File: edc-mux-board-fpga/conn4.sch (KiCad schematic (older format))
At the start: 24 parts

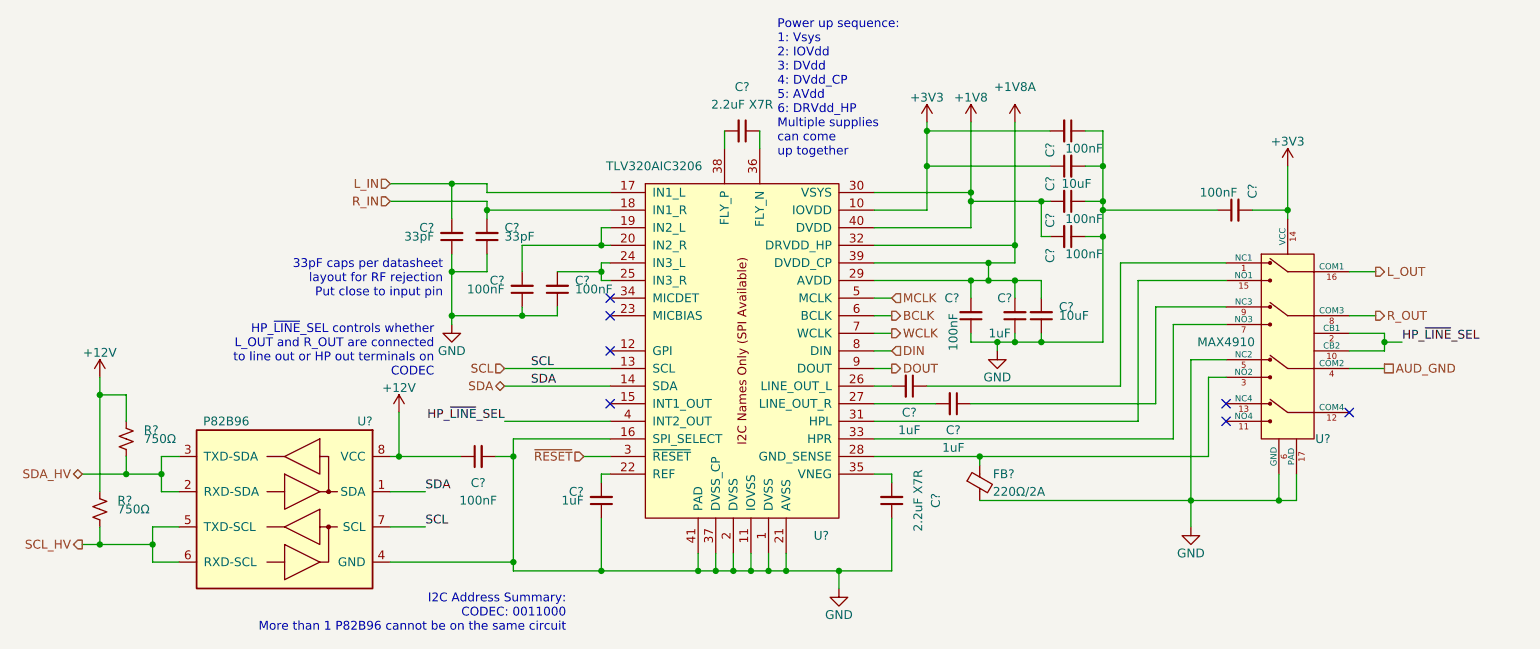
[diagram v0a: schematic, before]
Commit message: Finished FPGA and MCU interconnections.
Finished up interrupt wiring
Fixed a few missing connections
Annotated Schematic
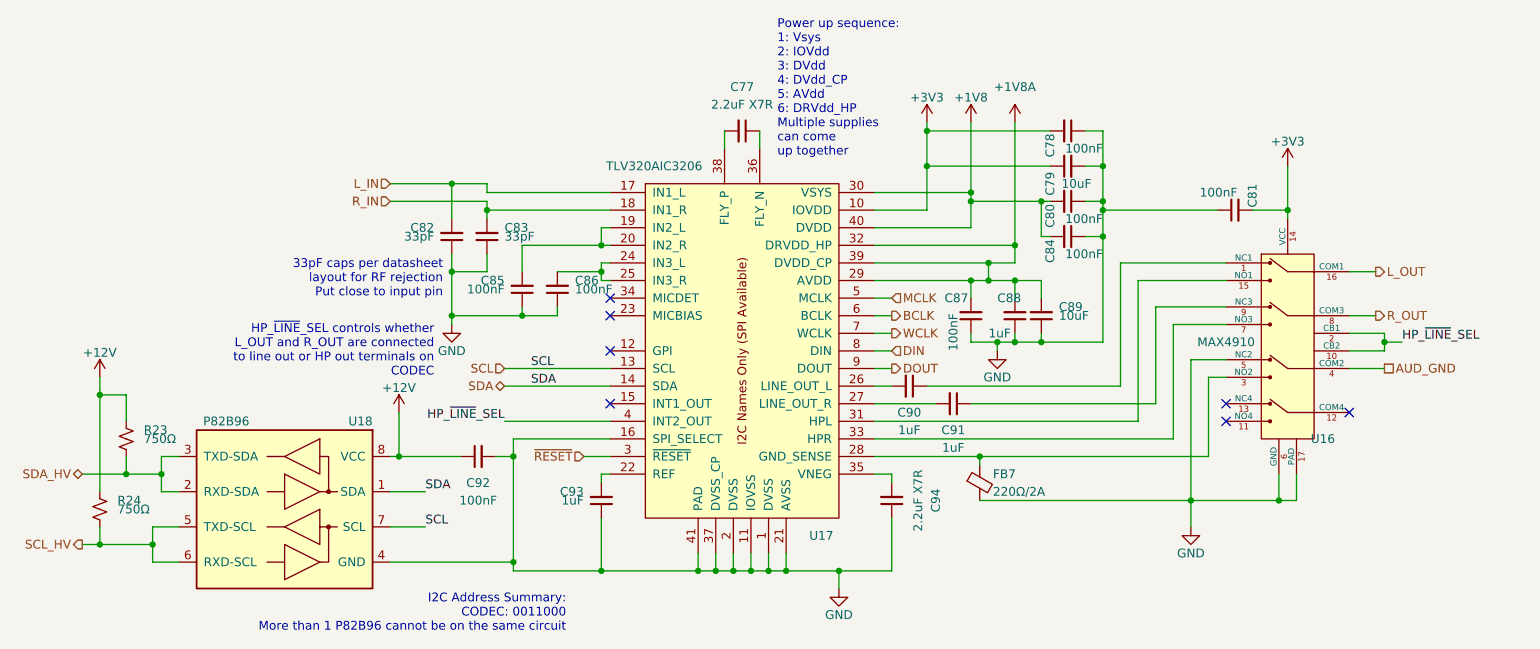
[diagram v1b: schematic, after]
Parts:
- removed C? (x2): 1uF, Capacitor_SMD:C_0805_2012Metric, symbol Device:C_Small
- removed C? (x2): 2.2uF X7R, Capacitor_SMD:C_0603_1608Metric, symbol Device:C_Small
- removed C? (x2): 1uF, Capacitor_SMD:C_0603_1608Metric, symbol Device:C_Small
- removed C? (x7): 100nF, Capacitor_SMD:C_0603_1608Metric, symbol Device:C_Small
- removed C? (x2): 33pF, Capacitor_SMD:C_0603_1608Metric, symbol Device:C_Small
- removed C? (x2): 10uF, Capacitor_SMD:C_1206_3216Metric, symbol Device:C_Small
- removed FB?: 220Ω/2A, Resistor_SMD:R_0603_1608Metric, symbol Device:Ferrite_Bead_Small
- removed R? (x2): 750Ω, Resistor_SMD:R_0603_1608Metric, symbol Device:R_Small_US
- removed U?: TLV320AIC3206, Package_DFN_QFN:UQFN-40-1EP_5x5mm_P0.4mm_EP3.8x3.8mm_ThermalVias, symbol SW-Texas:TLV320AIC3206
- removed U?: MAX4910, Package_DFN_QFN:TQFN-16-1EP_3x3mm_P0.5mm_EP1.23x1.23mm, symbol SW-dallas-semi-maxim:MAX4910
- removed U?: P82B96, Package_SO:TSSOP-8_3x3mm_P0.65mm, symbol Interface_Expansion:P82B96
- added C77, C94: 2.2uF X7R, Capacitor_SMD:C_0603_1608Metric, symbol Device:C_Small
- added C78, C80, C81, C84, C85, C86, C92: 100nF, Capacitor_SMD:C_0603_1608Metric, symbol Device:C_Small
- added C79, C89: 10uF, Capacitor_SMD:C_1206_3216Metric, symbol Device:C_Small
- added C82, C83: 33pF, Capacitor_SMD:C_0603_1608Metric, symbol Device:C_Small
- added C88, C93: 1uF, Capacitor_SMD:C_0603_1608Metric, symbol Device:C_Small
- added C90, C91: 1uF, Capacitor_SMD:C_0805_2012Metric, symbol Device:C_Small
- added FB7: 220Ω/2A, Resistor_SMD:R_0603_1608Metric, symbol Device:Ferrite_Bead_Small
- added R23, R24: 750Ω, Resistor_SMD:R_0603_1608Metric, symbol Device:R_Small_US
- added U16: MAX4910, Package_DFN_QFN:TQFN-16-1EP_3x3mm_P0.5mm_EP1.23x1.23mm, symbol SW-dallas-semi-maxim:MAX4910
- added U17: TLV320AIC3206, Package_DFN_QFN:UQFN-40-1EP_5x5mm_P0.4mm_EP3.8x3.8mm_ThermalVias, symbol SW-Texas:TLV320AIC3206
- added U18: P82B96, Package_SO:TSSOP-8_3x3mm_P0.65mm, symbol Interface_Expansion:P82B96
- gave numbers to parts that had none: 1
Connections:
- net +12V: now also C92.1, R23.1, R24.1, U18.8 (VCC)
- net +1V8: now also C80.2, C84.2, U17.30 (VSYS), U17.40 (DVDD)
- net +1V8A: now also C88.2, C89.2, U17.29 (AVDD), U17.32 (DRVDD_HP), U17.39 (DVDD_CP)
- net +3V3: now also C78.2, C79.1, C81.2, U16.14 (VCC), U17.10 (IOVDD)
- net AUD_GND: now also U16.4 (COM2)
- net BCLK: now also U17.6 (BCLK)
- net DIN: now also U17.8 (DIN)
- net DOUT: now also U17.9 (DOUT)
- net GND: now also C78.1, C79.2, C80.1, C81.1, C82.1, C83.1, C84.1, C85.1, C86.1, C88.1, C89.1, C92.2, C93.1, C94.1, FB7.2, U16.17 (PAD), U16.5 (NC2), U16.6 (GND), U17.1 (DVSS), U17.11 (IOVSS), U17.16 (SPI_SELECT), U17.2 (DVSS), U17.21 (AVSS), U17.37 (DVSS_CP), U17.41 (PAD), U18.4 (GND)
- net HP_~LINE~_SEL: now also U16.10 (CB2), U16.2 (CB1), U17.4 (INT2_OUT)
- net L_IN: now also C82.2, U17.17 (IN1_L)
- net L_OUT: now also U16.16 (COM1)
- net MCLK: now also U17.5 (MCLK)
- net R_IN: now also C83.2, U17.18 (IN1_R)
- net R_OUT: now also U16.8 (COM3)
- net SCL: now also U17.13 (SCL), U18.7 (SCL)
- net SCL_HV: now also R24.2, U18.5 (TXD-SCL), U18.6 (RXD-SCL)
- net SDA: now also U17.14 (SDA), U18.1 (SDA)
- net SDA_HV: now also R23.2, U18.2 (RXD-SDA), U18.3 (TXD-SDA)
- net WCLK: now also U17.7 (WCLK)
- net ~RESET: now also U17.3 (~RESET)
- new net: C90.1, U16.1 (NC1)
- new net: C90.2, U17.26 (LINE_OUT_L)
- new net: C91.1, U16.9 (NC3)
- new net: C91.2, U17.27 (LINE_OUT_R)
- new net: C85.2, U17.19 (IN2_L), U17.20 (IN2_R)
- new net: C93.2, U17.22 (REF)
- new net: C86.2, U17.24 (IN3_L), U17.25 (IN3_R)
- new net: FB7.1, U16.3 (NO2), U17.28 (GND_SENSE)
- new net: U16.15 (NO1), U17.31 (HPL)
- new net: U16.7 (NO3), U17.33 (HPR)
- new net: C94.2, U17.35 (VNEG)
- new net: C77.1, U17.36 (FLY_N)
- new net: C77.2, U17.38 (FLY_P)
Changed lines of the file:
@@
 $EndDescr
 $Comp
-L SW-Texas:TLV320AIC3206 U?
-U 1 1 5CE6F2E7
+L SW-Texas:TLV320AIC3206 U17
+U 1 1 5DAC04AE
 P 5200 3400
-F 0 "U?" H 5650 2350 50  0000 C CNN
+F 0 "U17" H 5650 2350 50  0000 C CNN
 F 1 "TLV320AIC3206" H 4700 4450 50  0000 C CNN
 F 2 "Package_DFN_QFN:UQFN-40-1EP_5x5mm_P0.4mm_EP3.8x3.8mm_ThermalVias" H 5250 4800 50  0001 C CNN
@@
 $EndComp
 $Comp
-L Device:C_Small C?
-U 1 1 5CE6F309
+L Device:C_Small C77
+U 1 1 5DAC04CA
 P 5200 2150
-F 0 "C?" V 4950 2150 50  0000 C CNN
+F 0 "C77" V 4950 2150 50  0000 C CNN
 F 1 "2.2uF X7R" V 5050 2150 50  0000 C CNN
 F 2 "Capacitor_SMD:C_0603_1608Metric" H 5200 2150 50  0001 C CNN
@@
 	5300 2250 5300 2150
 $Comp
-L Device:C_Small C?
-U 1 1 5CE6F311
+L Device:C_Small C94
+U 1 1 5DAC04D0
 P 6050 4250
-F 0 "C?" V 5800 4250 50  0000 C CNN
+F 0 "C94" V 5800 4250 50  0000 C CNN
 F 1 "2.2uF X7R" V 5900 4250 50  0000 C CNN
 F 2 "Capacitor_SMD:C_0603_1608Metric" H 6050 4250 50  0001 C CNN
@@
 	6050 4100 6050 4150
 $Comp
-L power:GND #PWR?
-U 1 1 5CE6F323
+L power:GND #PWR064
+U 1 1 5DAC04E1
 P 5750 4750
-F 0 "#PWR?" H 5750 4500 50  0001 C CNN
+F 0 "#PWR064" H 5750 4500 50  0001 C CNN
 F 1 "GND" H 5750 4600 50  0000 C CNN
 F 2 "" H 5750 4750 50  0001 C CNN
@@
 	5450 4650 5750 4650
 $Comp
-L Device:C_Small C?
-U 1 1 5CE6F329
+L Device:C_Small C93
+U 1 1 5DAC04F2
 P 4400 4250
-F 0 "C?" H 4500 4200 50  0000 L CNN
+F 0 "C93" H 4500 4200 50  0000 L CNN
 F 1 "1uF" H 4500 4250 50  0000 L CNN
 F 2 "Capacitor_SMD:C_0603_1608Metric" H 4400 4250 50  0001 C CNN
@@
 Connection ~ 4950 4650
 $Comp
-L Device:C_Small C?
-U 1 1 5CE6F348
+L Device:C_Small C85
+U 1 1 5DAC0500
 P 3950 3050
-F 0 "C?" H 4050 3000 50  0000 L CNN
+F 0 "C85" H 4050 3000 50  0000 L CNN
 F 1 "100nF" H 4050 3050 50  0000 L CNN
 F 2 "Capacitor_SMD:C_0603_1608Metric" H 3950 3050 50  0001 C CNN
@@
 $EndComp
 $Comp
-L Device:C_Small C?
-U 1 1 5CE6F363
+L Device:C_Small C86
+U 1 1 5DAC050A
 P 4150 3050
-F 0 "C?" H 4050 3000 50  0000 R CNN
+F 0 "C86" H 4050 3000 50  0000 R CNN
 F 1 "100nF" H 4050 3050 50  0000 R CNN
 F 2 "Capacitor_SMD:C_0603_1608Metric" H 4150 3050 50  0001 C CNN
@@
 Connection ~ 4400 2950
 $Comp
-L power:GND #PWR?
-U 1 1 5CE6F368
+L power:GND #PWR059
+U 1 1 5DAC051B
 P 3550 3250
-F 0 "#PWR?" H 3550 3000 50  0001 C CNN
+F 0 "#PWR059" H 3550 3000 50  0001 C CNN
 F 1 "GND" H 3550 3100 50  0000 C CNN
 F 2 "" H 3550 3250 50  0001 C CNN
@@
 	8650 3300 8850 3300
 $Comp
-L SW-dallas-semi-maxim:MAX4910 U?
-U 1 1 5CE6F375
+L SW-dallas-semi-maxim:MAX4910 U16
+U 1 1 5DAC052D
 P 8300 3350
-F 0 "U?" H 8500 2800 50  0000 C CNN
+F 0 "U16" H 8500 2800 50  0000 C CNN
 F 1 "MAX4910" H 7950 3350 50  0000 C CNN
 F 2 "Package_DFN_QFN:TQFN-16-1EP_3x3mm_P0.5mm_EP1.23x1.23mm" H 9950 4500 50  0001 C CNN
@@
 	7750 3450 7750 4250
 $Comp
-L power:GND #PWR?
-U 1 1 5CE6F387
+L power:GND #PWR063
+U 1 1 5DAC053B
 P 7750 4400
-F 0 "#PWR?" H 7750 4150 50  0001 C CNN
+F 0 "#PWR063" H 7750 4150 50  0001 C CNN
 F 1 "GND" H 7750 4250 50  0000 C CNN
 F 2 "" H 7750 4400 50  0001 C CNN
@@
 	8650 3500 8850 3500
 $Comp
-L Device:Ferrite_Bead_Small FB?
-U 1 1 5CE6F39A
+L Device:Ferrite_Bead_Small FB7
+U 1 1 5DAC0544
 P 6550 4150
-F 0 "FB?" H 6625 4200 50  0000 L CNN
+F 0 "FB7" H 6625 4200 50  0000 L CNN
 F 1 "220Ω/2A" H 6625 4100 50  0000 L CNN
 F 2 "Resistor_SMD:R_0603_1608Metric" V 6480 4150 50  0001 C CNN
@@
 	3750 2600 4450 2600
 $Comp
-L Device:C_Small C?
-U 1 1 5CE6F3AC
+L Device:C_Small C82
+U 1 1 5DAC0552
 P 3550 2750
-F 0 "C?" H 3650 2700 50  0000 L CNN
+F 0 "C82" H 3650 2700 50  0000 L CNN
 F 1 "33pF" H 3650 2750 50  0000 L CNN
 F 2 "Capacitor_SMD:C_0603_1608Metric" H 3550 2750 50  0001 C CNN
@@
 	3200 2550 3750 2550
 $Comp
-L Device:C_Small C?
-U 1 1 5CE6F3B7
+L Device:C_Small C83
+U 1 1 5DAC0563
 P 3750 2750
-F 0 "C?" H 3650 2700 50  0000 R CNN
+F 0 "C83" H 3650 2700 50  0000 R CNN
 F 1 "33pF" H 3650 2750 50  0000 R CNN
 F 2 "Capacitor_SMD:C_0603_1608Metric" H 3750 2750 50  0001 C CNN
@@
 	5950 3000 6500 3000
 $Comp
-L SW-power:+1V8A #+1V8A?
+L SW-power:+1V8A #+1V8A06
 U 1 1 5CE6F3C8
 P 6750 2100
-F 0 "#+1V8A?" H 7500 1800 60  0001 C CNN
+F 0 "#+1V8A06" H 7500 1800 60  0001 C CNN
 F 1 "+1V8A" H 6750 2300 50  0000 C CNN
 F 2 "" H 6750 2100 60  0001 C CNN
@@
 $EndComp
 $Comp
-L power:+1V8 #PWR?
-U 1 1 5CE6F3D1
+L power:+1V8 #PWR057
+U 1 1 5DAC0580
 P 6500 2100
-F 0 "#PWR?" H 6500 1950 50  0001 C CNN
+F 0 "#PWR057" H 6500 1950 50  0001 C CNN
 F 1 "+1V8" H 6500 2240 50  0000 C CNN
 F 2 "" H 6500 2100 50  0001 C CNN
@@
 	6750 2800 6750 2900
 $Comp
-L power:+3V3 #PWR?
-U 1 1 5CE6F3E5
+L power:+3V3 #PWR056
+U 1 1 5DAC0592
 P 6250 2100
-F 0 "#PWR?" H 6250 1950 50  0001 C CNN
+F 0 "#PWR056" H 6250 1950 50  0001 C CNN
 F 1 "+3V3" H 6250 2240 50  0000 C CNN
 F 2 "" H 6250 2100 50  0001 C CNN
@@
 	6250 2600 6250 2350
 $Comp
-L Device:C_Small C?
-U 1 1 5CE6F3F4
+L Device:C_Small C88
+U 1 1 5DAC05A5
 P 6750 3200
-F 0 "C?" H 6850 3100 50  0000 R CNN
+F 0 "C88" H 6850 3100 50  0000 R CNN
 F 1 "1uF" H 6900 3300 50  0000 R CNN
 F 2 "Capacitor_SMD:C_0603_1608Metric" H 6750 3200 50  0001 C CNN
@@
 $EndComp
 $Comp
-L power:GND #PWR?
-U 1 1 5CE6F403
+L power:GND #PWR060
+U 1 1 5DAC05B6
 P 6650 3400
-F 0 "#PWR?" H 6650 3150 50  0001 C CNN
+F 0 "#PWR060" H 6650 3150 50  0001 C CNN
 F 1 "GND" H 6650 3250 50  0000 C CNN
 F 2 "" H 6650 3400 50  0001 C CNN
@@
 $EndComp
 $Comp
-L Device:C_Small C?
-U 1 1 5CE6F40F
+L Device:C_Small C89
+U 1 1 5DAC05BE
 P 6900 3200
-F 0 "C?" H 6800 3150 50  0000 R CNN
+F 0 "C89" H 6800 3150 50  0000 R CNN
 F 1 "10uF" H 6800 3200 50  0000 R CNN
 F 2 "Capacitor_SMD:C_1206_3216Metric" H 6900 3200 50  0001 C CNN
@@
 $EndComp
 $Comp
-L Device:C_Small C?
+L Device:C_Small C87
 U 1 1 5CE6F425
 P 6500 3200
-F 0 "C?" H 6650 3100 50  0000 R CNN
+F 0 "C87" H 6650 3100 50  0000 R CNN
 F 1 "100nF" V 6600 3400 50  0000 R CNN
 F 2 "Capacitor_SMD:C_0603_1608Metric" H 6500 3200 50  0001 C CNN
@@
 	6650 3350 6750 3350
 $Comp
-L Device:C_Small C?
-U 1 1 5CE6F42F
+L Device:C_Small C78
+U 1 1 5DAC05DF
 P 7050 2150
-F 0 "C?" H 7200 2050 50  0000 R CNN
+F 0 "C78" H 7200 2050 50  0000 R CNN
 F 1 "100nF" V 7150 2350 50  0000 R CNN
 F 2 "Capacitor_SMD:C_0603_1608Metric" H 7050 2150 50  0001 C CNN
@@
 $EndComp
 $Comp
-L Device:C_Small C?
-U 1 1 5CE6F439
+L Device:C_Small C79
+U 1 1 5DAC05EB
 P 7050 2350
-F 0 "C?" H 6950 2450 50  0000 C CNN
+F 0 "C79" H 6950 2450 50  0000 C CNN
 F 1 "10uF" V 6950 2300 50  0000 C CNN
 F 2 "Capacitor_SMD:C_1206_3216Metric" H 7050 2350 50  0001 C CNN
@@
 	6250 2150 6250 2100
 $Comp
-L Device:C_Small C?
-U 1 1 5CE6F451
+L Device:C_Small C80
+U 1 1 5DAC0605
 P 7050 2550
-F 0 "C?" H 7200 2450 50  0000 R CNN
+F 0 "C80" H 7200 2450 50  0000 R CNN
 F 1 "100nF" V 7150 2750 50  0000 R CNN
 F 2 "Capacitor_SMD:C_0603_1608Metric" H 7050 2550 50  0001 C CNN
@@
 	6500 2550 6500 2500
 $Comp
-L Device:C_Small C?
-U 1 1 5CE6F456
+L Device:C_Small C84
+U 1 1 5DAC0608
 P 7050 2750
-F 0 "C?" H 7200 2650 50  0000 R CNN
+F 0 "C84" H 7200 2650 50  0000 R CNN
 F 1 "100nF" V 7150 2950 50  0000 R CNN
 F 2 "Capacitor_SMD:C_0603_1608Metric" H 7050 2750 50  0001 C CNN
@@
 NoConn ~ 8650 3750
 $Comp
-L Device:C_Small C?
-U 1 1 5CE6F46F
+L Device:C_Small C81
+U 1 1 5DAC0621
 P 8000 2600
-F 0 "C?" H 8150 2500 50  0000 R CNN
+F 0 "C81" H 8150 2500 50  0000 R CNN
 F 1 "100nF" V 8100 2800 50  0000 R CNN
 F 2 "Capacitor_SMD:C_0603_1608Metric" H 8000 2600 50  0001 C CNN
@@
 $EndComp
 $Comp
-L power:+3V3 #PWR?
-U 1 1 5CE6F47E
+L power:+3V3 #PWR058
+U 1 1 5DAC062A
 P 8300 2350
-F 0 "#PWR?" H 8300 2200 50  0001 C CNN
+F 0 "#PWR058" H 8300 2200 50  0001 C CNN
 F 1 "+3V3" H 8300 2490 50  0000 C CNN
 F 2 "" H 8300 2350 50  0001 C CNN
@@
 	8250 4250 8350 4250
 $Comp
-L Interface_Expansion:P82B96 U?
-U 1 1 5CE6F489
+L Interface_Expansion:P82B96 U18
+U 1 1 5DAC063F
 P 2600 4300
-F 0 "U?" H 2100 4800 50  0000 L CNN
+F 0 "U18" H 2100 4800 50  0000 L CNN
 F 1 "P82B96" H 2800 4800 50  0000 L CNN
 F 2 "Package_SO:TSSOP-8_3x3mm_P0.65mm" H 2600 4300 50  0001 C CNN
@@
 $EndComp
 $Comp
-L power:+12V #PWR?
-U 1 1 5CE6F490
+L power:+12V #PWR061
+U 1 1 5DAC0643
 P 1550 3550
-F 0 "#PWR?" H 1550 3400 50  0001 C CNN
+F 0 "#PWR061" H 1550 3400 50  0001 C CNN
 F 1 "+12V" H 1550 3690 50  0000 C CNN
 F 2 "" H 1550 3550 50  0001 C CNN
@@
 	1900 4100 1900 4200
 $Comp
-L Device:R_Small_US R?
-U 1 1 5CE6F4C1
+L Device:R_Small_US R23
+U 1 1 5DAC065A
 P 1700 3900
-F 0 "R?" H 1800 3950 50  0000 L CNN
+F 0 "R23" H 1800 3950 50  0000 L CNN
 F 1 "750Ω" H 1800 3900 50  0000 L CNN
 F 2 "Resistor_SMD:R_0603_1608Metric" H 1700 3900 50  0001 C CNN
@@
 $EndComp
 $Comp
-L Device:R_Small_US R?
-U 1 1 5CE6F4D0
+L Device:R_Small_US R24
+U 1 1 5DAC0666
 P 1550 4300
-F 0 "R?" H 1650 4350 50  0000 L CNN
+F 0 "R24" H 1650 4350 50  0000 L CNN
 F 1 "750Ω" H 1650 4300 50  0000 L CNN
 F 2 "Resistor_SMD:R_0603_1608Metric" H 1550 4300 50  0001 C CNN
@@
 	1700 4100 1900 4100
 $Comp
-L power:+12V #PWR?
-U 1 1 5CE6F4E1
+L power:+12V #PWR062
+U 1 1 5DAC067C
 P 3250 3750
-F 0 "#PWR?" H 3250 3600 50  0001 C CNN
+F 0 "#PWR062" H 3250 3600 50  0001 C CNN
 F 1 "+12V" H 3250 3890 50  0000 C CNN
 F 2 "" H 3250 3750 50  0001 C CNN
@@
 	3200 4400 3400 4400
 $Comp
-L Device:C_Small C?
-U 1 1 5CE6F4F3
+L Device:C_Small C92
+U 1 1 5DAC067E
 P 3700 4000
-F 0 "C?" V 3550 4000 50  0000 C CNN
+F 0 "C92" V 3550 4000 50  0000 C CNN
 F 1 "100nF" V 3450 4000 50  0000 C CNN
 F 2 "Capacitor_SMD:C_0603_1608Metric" H 3700 4000 50  0001 C CNN
@@
 	1450 4500 1550 4500
 $Comp
-L Device:C_Small C?
-U 1 1 5CE6F2C0
+L Device:C_Small C90
+U 1 1 5DAC0499
 P 6150 3600
-F 0 "C?" V 6300 3600 50  0000 C CNN
+F 0 "C90" V 6300 3600 50  0000 C CNN
 F 1 "1uF" V 6400 3600 50  0000 C CNN
 F 2 "Capacitor_SMD:C_0805_2012Metric" H 6150 3600 50  0001 C CNN
@@
 $EndComp
 $Comp
-L Device:C_Small C?
-U 1 1 5CE6F2D4
+L Device:C_Small C91
+U 1 1 5DAC04AB
 P 6400 3700
-F 0 "C?" V 6550 3700 50  0000 C CNN
+F 0 "C91" V 6550 3700 50  0000 C CNN
 F 1 "1uF" V 6650 3700 50  0000 C CNN
 F 2 "Capacitor_SMD:C_0805_2012Metric" H 6400 3700 50  0001 C CNN

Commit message: assigned more footprints
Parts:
- C79, C89: value 10uF -> 10uF X7R
- C88, C93: value 1uF -> 1uF X7R
- C90, C91: value 1uF -> 1uF X7R flex
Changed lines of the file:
@@
 P 4400 4250
 F 0 "C93" H 4500 4200 50  0000 L CNN
-F 1 "1uF" H 4500 4250 50  0000 L CNN
+F 1 "1uF X7R" H 4500 4250 50  0000 L CNN
 F 2 "Capacitor_SMD:C_0603_1608Metric" H 4400 4250 50  0001 C CNN
 F 3 "~" H 4400 4250 50  0001 C CNN
@@
 P 6750 3200
 F 0 "C88" H 6850 3100 50  0000 R CNN
-F 1 "1uF" H 6900 3300 50  0000 R CNN
+F 1 "1uF X7R" H 6900 3300 50  0000 R CNN
 F 2 "Capacitor_SMD:C_0603_1608Metric" H 6750 3200 50  0001 C CNN
 F 3 "~" H 6750 3200 50  0001 C CNN
@@
 P 6900 3200
 F 0 "C89" H 6800 3150 50  0000 R CNN
-F 1 "10uF" H 6800 3200 50  0000 R CNN
+F 1 "10uF X7R" H 6800 3200 50  0000 R CNN
 F 2 "Capacitor_SMD:C_1206_3216Metric" H 6900 3200 50  0001 C CNN
 F 3 "~" H 6900 3200 50  0001 C CNN
@@
 P 7050 2350
 F 0 "C79" H 6950 2450 50  0000 C CNN
-F 1 "10uF" V 6950 2300 50  0000 C CNN
+F 1 "10uF X7R" V 6950 2300 50  0000 C CNN
 F 2 "Capacitor_SMD:C_1206_3216Metric" H 7050 2350 50  0001 C CNN
 F 3 "~" H 7050 2350 50  0001 C CNN
@@
 P 6150 3600
 F 0 "C90" V 6300 3600 50  0000 C CNN
-F 1 "1uF" V 6400 3600 50  0000 C CNN
+F 1 "1uF X7R flex" V 6400 3600 50  0000 C CNN
 F 2 "Capacitor_SMD:C_0805_2012Metric" H 6150 3600 50  0001 C CNN
 F 3 "~" H 6150 3600 50  0001 C CNN
@@
 P 6400 3700
 F 0 "C91" V 6550 3700 50  0000 C CNN
-F 1 "1uF" V 6650 3700 50  0000 C CNN
+F 1 "1uF X7R flex" V 6650 3700 50  0000 C CNN
 F 2 "Capacitor_SMD:C_0805_2012Metric" H 6400 3700 50  0001 C CNN
 F 3 "~" H 6400 3700 50  0001 C CNN
